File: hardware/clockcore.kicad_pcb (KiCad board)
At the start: 2 copper layers, 75 x 40 mm, 61 parts, among them J1 Header, J2 Ext, J3 JTAG, J7 GCT_USB4108-GF-A, Q1 MBT3904DW1T1G, SW1 Reset, SW2 Boot, U1 AP2114H-3_3TRG1, U2 ‎SN74HCT245PWR‎, U3 ESP32-WROOM-32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

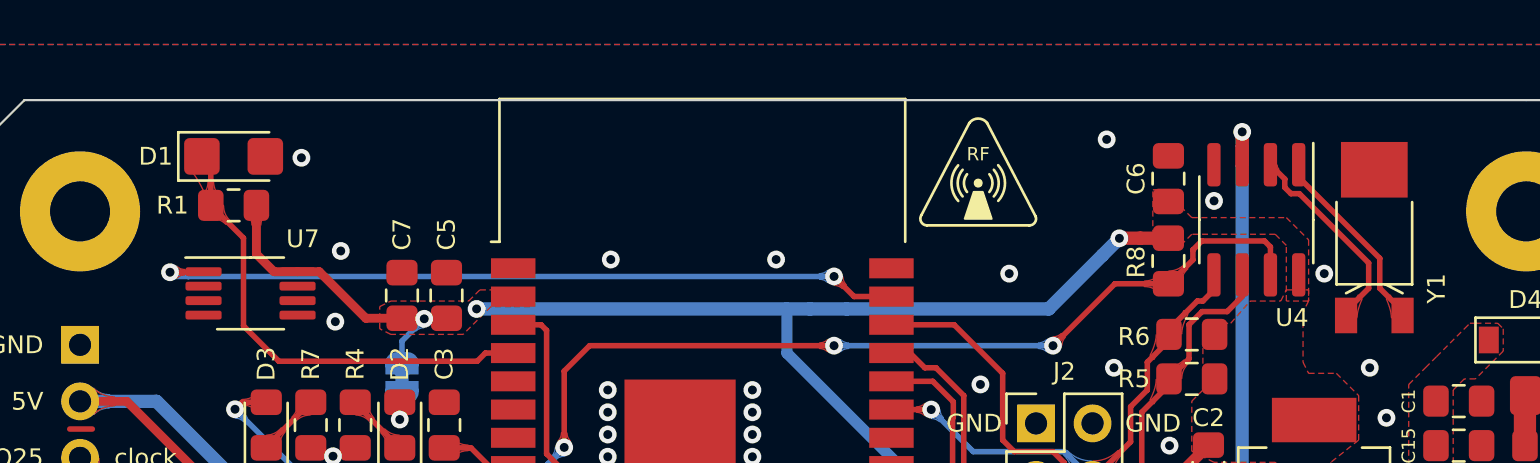
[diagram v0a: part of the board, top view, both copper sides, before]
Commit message: hardware: tidy up, fix photodiode, (re)export (i)boms and schematics
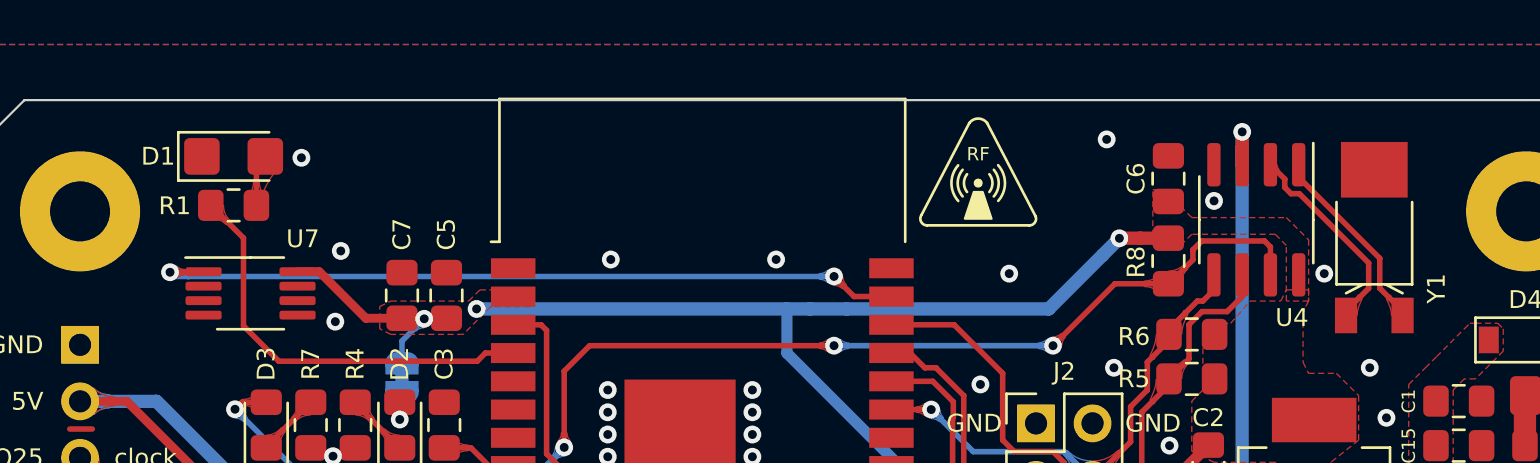
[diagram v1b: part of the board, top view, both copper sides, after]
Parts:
- BT1: value 12mm Coin Cell -> Keystone 1058 (CR2032)
- D1: value Ambient Light Sensor -> Photodiode
- D2: value PWR LED -> PWR RED
- D3: value GPIO LED -> USR GRN
- R1: value 4.7kΩ -> 1MΩ
- R4: value 1kΩ -> 2.2kΩ
- turned R1 to 0 degrees
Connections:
- D1 pad 1: LIGHT -> GND
- D1 pad 2: GND -> Net-(D1-Pad2)
- R1 pad 1: +3V3 -> LIGHT
- R1 pad 2: LIGHT -> Net-(D1-Pad2)
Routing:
- net +3V3: track 126.8 -> 122.5 mm
- net Net-(D1-Pad2): track 0.00 -> 2.37 mm
- net LIGHT: track 21.3 -> 19.0 mm
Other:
- board text added: "Clock Core v1.1 github.com/ansemjo/chronovfd"
- board text removed: "Clock Core v1.0 github.com/ansemjo/chronovfd"
